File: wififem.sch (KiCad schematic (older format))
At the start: 44 parts, among them J1 Conn_Coaxial, J2 Conn_Coaxial, J3 Conn_Coaxial, J4 Conn_01x05, U1 MCP6566, U2 74HCT04, U3 SE2611T, U4 AP1117-15

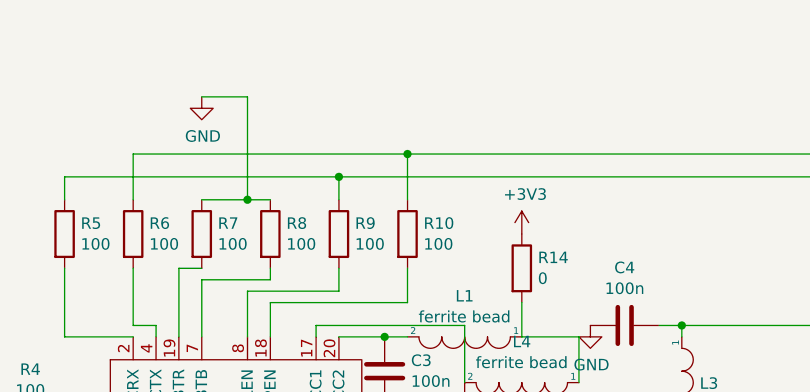
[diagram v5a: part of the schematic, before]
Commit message: Add LNA on/off jumper
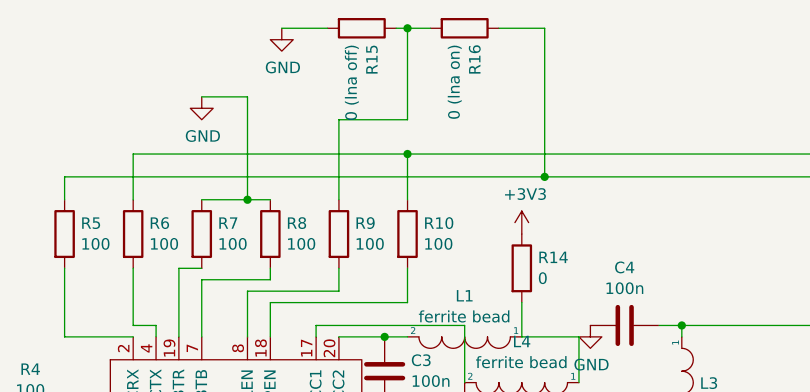
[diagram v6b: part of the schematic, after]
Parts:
- added R15: 0 (lna off), Resistors_SMD:R_0603, symbol device:R
- added R16: 0 (lna on), Resistors_SMD:R_0603, symbol device:R
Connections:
- wire segments 85 -> 91
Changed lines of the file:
@@
 	5700 2000 5700 1800
 Wire Wire Line
-	5700 1800 6100 1800
-Wire Wire Line
 	6100 1800 6100 1700
 Wire Wire Line
@@
 Wire Wire Line
 	5800 1850 5800 2000
-Wire Wire Line
-	6100 1400 6100 1300
 Wire Wire Line
 	4900 1300 8450 1300
@@
 	8450 1300 8450 3950
 Connection ~ 8450 3950
-Connection ~ 6100 1300
 Wire Wire Line
 	9100 3950 9100 1200
@@
 Connection ~ 7600 1950
 $Comp
-L power:GND #PWR?
+L power:GND #PWR028
 U 1 1 5A15FD74
 P 5300 3200
-F 0 "#PWR?" H 5300 2950 50  0001 C CNN
+F 0 "#PWR028" H 5300 2950 50  0001 C CNN
 F 1 "GND" H 5305 3027 50  0000 C CNN
 F 2 "" H 5300 3200 50  0001 C CNN
@@
 Wire Wire Line
 	5300 3200 5300 3150
+$Comp
+L device:R R15
+U 1 1 5A16EBBC
+P 6200 650
+F 0 "R15" H 6270 696 50  0000 L CNN
+F 1 "0 (lna off)" H 6270 605 50  0000 L CNN
+F 2 "Resistors_SMD:R_0603" V 6130 650 50  0001 C CNN
+F 3 "" H 6200 650 50  0001 C CNN
+	1    6200 650
+	0    1    1    0
+$EndComp
+$Comp
+L power:GND #PWR030
+U 1 1 5A172D6A
+P 5850 650
+F 0 "#PWR030" H 5850 400 50  0001 C CNN
+F 1 "GND" H 5855 477 50  0000 C CNN
+F 2 "" H 5850 650 50  0001 C CNN
+F 3 "" H 5850 650 50  0001 C CNN
+	1    5850 650
+	1    0    0    -1
+$EndComp
+Wire Wire Line
+	5850 650  6050 650
+Wire Wire Line
+	5700 1800 6100 1800
+$Comp
+L device:R R16
+U 1 1 5A17F845
+P 6650 650
+F 0 "R16" H 6720 696 50  0000 L CNN
+F 1 "0 (lna on)" H 6720 605 50  0000 L CNN
+F 2 "Resistors_SMD:R_0603" V 6580 650 50  0001 C CNN
+F 3 "" H 6650 650 50  0001 C CNN
+	1    6650 650
+	0    1    1    0
+$EndComp
+Wire Wire Line
+	7000 1300 7000 650
+Wire Wire Line
+	7000 650  6800 650
+Connection ~ 7000 1300
+Wire Wire Line
+	6100 1400 6100 1050
+Wire Wire Line
+	6100 1050 6400 1050
+Wire Wire Line
+	6400 1050 6400 650
+Wire Wire Line
+	6350 650  6500 650
+Connection ~ 6400 650
 $EndSCHEMATC

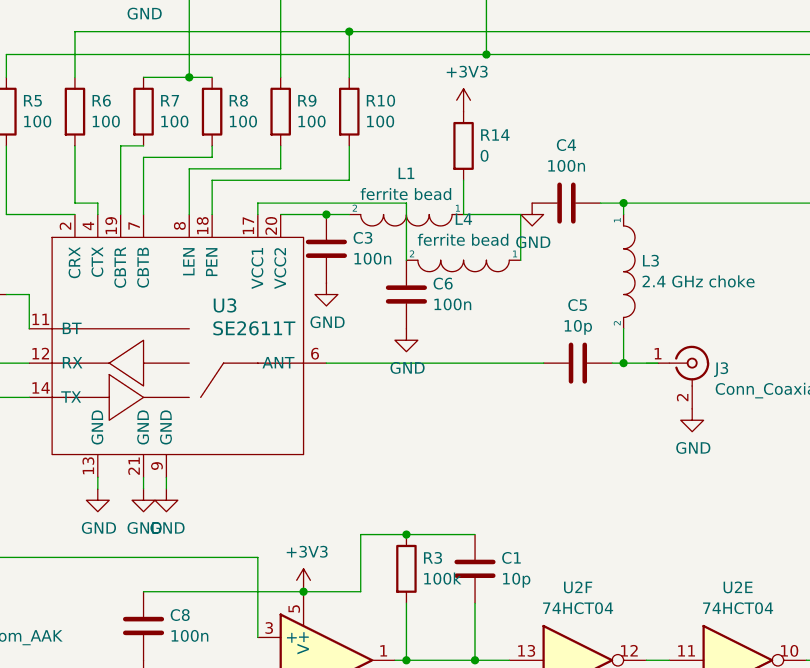
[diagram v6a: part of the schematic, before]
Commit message: Power supply decoupling as suggested
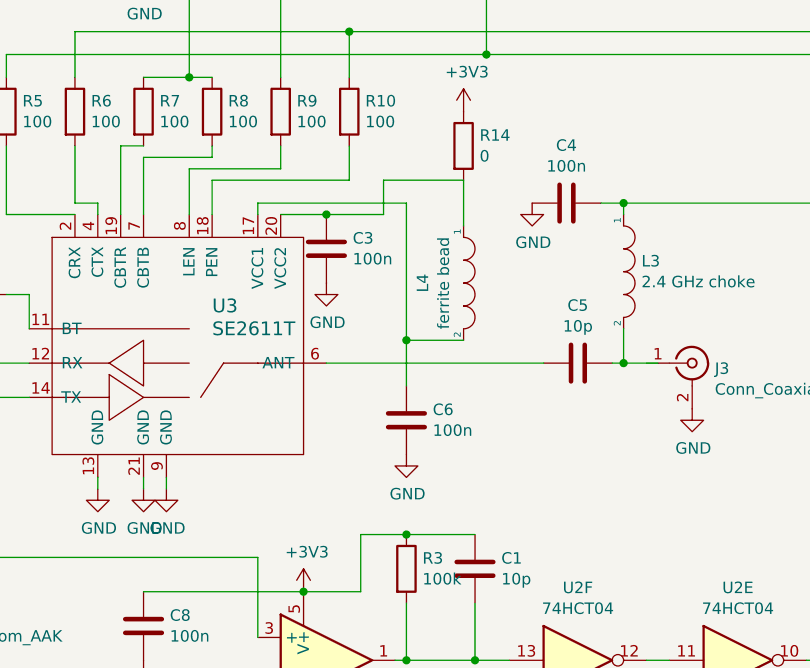
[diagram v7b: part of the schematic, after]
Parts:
- removed L1: ferrite bead, Inductors_SMD:L_0805_HandSoldering, symbol pspice:INDUCTOR
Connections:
- wire segments 91 -> 92
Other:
- moved on the sheet: C6, L4
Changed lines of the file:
@@
-$EndComp
-$Comp
-L pspice:INDUCTOR L1
-U 1 1 5A17AD26
-P 6650 2000
-F 0 "L1" H 6650 1822 50  0000 C CNN
-F 1 "ferrite bead" H 6650 1913 50  0000 C CNN
-F 2 "Inductors_SMD:L_0805_HandSoldering" H 6650 2000 50  0001 C CNN
-F 3 "" H 6650 2000 50  0001 C CNN
-	1    6650 2000
-	-1   0    0    1
 $EndComp
 $Comp
@@
 L device:C C6
 U 1 1 5A184860
-P 6650 2350
-F 0 "C6" H 6535 2304 50  0000 R CNN
-F 1 "100n" H 6535 2395 50  0000 R CNN
-F 2 "Capacitors_SMD:C_0805_HandSoldering" H 6688 2200 50  0001 C CNN
-F 3 "" H 6650 2350 50  0001 C CNN
-	1    6650 2350
+P 6650 2900
+F 0 "C6" H 6535 2854 50  0000 R CNN
+F 1 "100n" H 6535 2945 50  0000 R CNN
+F 2 "Capacitors_SMD:C_0805_HandSoldering" H 6688 2750 50  0001 C CNN
+F 3 "" H 6650 2900 50  0001 C CNN
+	1    6650 2900
 	-1   0    0    1
 $EndComp
@@
 L power:GND #PWR016
 U 1 1 5A1848E9
-P 6650 2500
-F 0 "#PWR016" H 6650 2250 50  0001 C CNN
-F 1 "GND" H 6655 2327 50  0000 C CNN
-F 2 "" H 6650 2500 50  0001 C CNN
-F 3 "" H 6650 2500 50  0001 C CNN
-	1    6650 2500
+P 6650 3050
+F 0 "#PWR016" H 6650 2800 50  0001 C CNN
+F 1 "GND" H 6655 2877 50  0000 C CNN
+F 2 "" H 6650 3050 50  0001 C CNN
+F 3 "" H 6650 3050 50  0001 C CNN
+	1    6650 3050
 	1    0    0    -1
 $EndComp
@@
 L pspice:INDUCTOR L4
 U 1 1 5A18492E
-P 6900 2200
-F 0 "L4" H 6900 2022 50  0000 C CNN
-F 1 "ferrite bead" H 6900 2113 50  0000 C CNN
-F 2 "Inductors_SMD:L_0805_HandSoldering" H 6900 2200 50  0001 C CNN
-F 3 "" H 6900 2200 50  0001 C CNN
-	1    6900 2200
-	-1   0    0    1
+P 6900 2300
+F 0 "L4" H 6900 2122 50  0000 C CNN
+F 1 "ferrite bead" H 6900 2213 50  0000 C CNN
+F 2 "Inductors_SMD:L_0805_HandSoldering" H 6900 2300 50  0001 C CNN
+F 3 "" H 6900 2300 50  0001 C CNN
+	1    6900 2300
+	0    1    1    0
 $EndComp
 $Comp
@@
 	-1   0    0    1
 $EndComp
-Wire Wire Line
-	8400 3950 8500 3950
-Wire Wire Line
-	7800 3950 7700 3950
-Wire Wire Line
-	6600 3950 7100 3950
-Wire Wire Line
-	6950 3700 6950 3950
-Connection ~ 6950 3950
-Wire Wire Line
-	6650 3700 6650 3950
-Connection ~ 6650 3950
-Wire Wire Line
-	6450 3400 6950 3400
-Connection ~ 6650 3400
-Wire Wire Line
-	5500 3650 6450 3650
-Wire Wire Line
-	6450 3400 6450 3650
-Wire Wire Line
-	5500 3200 5500 3150
-Wire Wire Line
-	5600 3200 5600 3150
-Wire Wire Line
-	5200 2000 4900 2000
-Wire Wire Line
-	4900 2000 4900 1700
-Wire Wire Line
-	5200 1700 5200 1950
-Wire Wire Line
-	5200 1950 5300 1950
-Wire Wire Line
-	5300 1950 5300 2000
-Wire Wire Line
-	5400 2000 5400 1700
-Wire Wire Line
-	5400 1700 5500 1700
-Wire Wire Line
-	5800 1700 5800 1750
-Wire Wire Line
-	5800 1750 5500 1750
-Wire Wire Line
-	5500 1750 5500 2000
-Wire Wire Line
-	5700 2000 5700 1800
-Wire Wire Line
-	6100 1800 6100 1700
-Wire Wire Line
-	6400 1700 6400 1850
-Wire Wire Line
-	6400 1850 5800 1850
-Wire Wire Line
-	5800 1850 5800 2000
-Wire Wire Line
-	4900 1300 8450 1300
-Wire Wire Line
-	4900 1300 4900 1400
-Wire Wire Line
-	5200 1400 5200 1200
-Wire Wire Line
-	5200 1200 9100 1200
-Wire Wire Line
-	6400 1200 6400 1400
-Wire Wire Line
-	5500 1400 5800 1400
-Wire Wire Line
-	5700 1400 5700 950
-Wire Wire Line
-	5700 950  5500 950
-Connection ~ 5700 1400
-Wire Wire Line
-	8450 1300 8450 3950
-Connection ~ 8450 3950
-Wire Wire Line
-	9100 3950 9100 1200
-Connection ~ 6400 1200
-Wire Wire Line
-	7550 2650 7750 2650
-Wire Wire Line
-	7250 2650 6300 2650
-Connection ~ 7600 2650
-Wire Wire Line
-	7500 1950 9250 1950
-Wire Wire Line
-	7600 2500 7600 2650
-Wire Wire Line
-	4100 2800 5000 2800
-Wire Wire Line
-	3800 2650 5000 2650
-Wire Wire Line
-	4550 2350 4600 2350
-Wire Wire Line
-	5000 2500 5000 2350
-Wire Wire Line
-	5000 2350 4900 2350
-Connection ~ 6300 2000
-Wire Wire Line
-	6100 2000 6400 2000
-Wire Wire Line
-	6900 2000 7150 2000
-Wire Wire Line
-	7150 2000 7150 2200
-Wire Wire Line
-	6650 2200 6650 1950
-Wire Wire Line
-	6650 1950 6000 1950
-Wire Wire Line
-	6000 1950 6000 2000
-Wire Wire Line
-	4150 2800 4150 2950
-Wire Wire Line
-	4150 3250 4150 3500
-Wire Wire Line
-	3900 3500 4350 3500
-Wire Wire Line
-	3900 4100 4350 4100
-Wire Wire Line
-	4650 3500 6000 3500
-Wire Wire Line
-	6000 3500 6000 3850
-Wire Wire Line
-	6000 4050 4650 4050
-Wire Wire Line
-	4650 4050 4650 4100
-Connection ~ 4150 3500
-Connection ~ 4150 4100
-Wire Wire Line
-	3600 3500 3600 4100
-Wire Wire Line
-	3400 3850 3600 3850
-Connection ~ 3600 3850
-Wire Wire Line
-	6000 4900 5900 4900
-Wire Wire Line
-	5600 5250 5600 5200
-Wire Wire Line
-	4250 4900 5300 4900
-Connection ~ 6200 3650
-Wire Wire Line
-	7650 4550 7100 4550
-Wire Wire Line
-	7100 4550 7100 4850
-Wire Wire Line
-	7650 5550 7100 5550
-Wire Wire Line
-	7100 5550 7100 5150
-Connection ~ 4150 2800
-Connection ~ 4700 2800
-Wire Wire Line
-	9650 2100 9650 3300
-Connection ~ 9650 2700
-Wire Wire Line
-	6900 1850 6900 2000
-Wire Wire Line
-	3550 4550 3550 5000
-Wire Wire Line
-	3550 4950 3500 4950
-Wire Wire Line
-	3550 4550 3500 4550
-Connection ~ 3550 4950
-Wire Wire Line
-	3500 4750 3550 4750
-Connection ~ 3550 4750
-Wire Wire Line
-	3500 4650 3750 4650
-Wire Wire Line
-	3750 4650 3750 4550
-Wire Wire Line
-	3500 4850 3750 4850
-Wire Wire Line
-	3750 4850 3750 4900
-Connection ~ 5000 4900
-Connection ~ 4500 4900
-Wire Wire Line
-	4250 4550 6800 4550
-Wire Wire Line
-	6800 4550 6800 5850
-Wire Wire Line
-	6800 5850 9250 5850
-Wire Wire Line
-	9250 5850 9250 1950
 $Comp
 L pspice:INDUCTOR L2
@@
 	1    0    0    -1
 $EndComp
-Wire Wire Line
-	7600 2000 7600 1950
-Connection ~ 7600 1950
 $Comp
 L power:GND #PWR028
@@
 	1    0    0    -1
 $EndComp
-Wire Wire Line
-	5300 3200 5300 3150
 $Comp
 L device:R R15
@@
 	1    0    0    -1
 $EndComp
-Wire Wire Line
-	5850 650  6050 650
-Wire Wire Line
-	5700 1800 6100 1800
 $Comp
 L device:R R16
@@
 $EndComp
 Wire Wire Line
+	8400 3950 8500 3950
+Wire Wire Line
+	7800 3950 7700 3950
+Wire Wire Line
+	6600 3950 7100 3950
+Wire Wire Line
+	6950 3700 6950 3950
+Connection ~ 6950 3950
+Wire Wire Line
+	6650 3700 6650 3950
+Connection ~ 6650 3950
+Wire Wire Line
+	6450 3400 6950 3400
+Connection ~ 6650 3400
+Wire Wire Line
+	5500 3650 6450 3650
+Wire Wire Line
+	6450 3400 6450 3650
+Wire Wire Line
+	5500 3200 5500 3150
+Wire Wire Line
+	5600 3200 5600 3150
+Wire Wire Line
+	5200 2000 4900 2000
+Wire Wire Line
+	4900 2000 4900 1700
+Wire Wire Line
+	5200 1700 5200 1950
+Wire Wire Line
+	5200 1950 5300 1950
+Wire Wire Line
+	5300 1950 5300 2000
+Wire Wire Line
+	5400 2000 5400 1700
+Wire Wire Line
+	5400 1700 5500 1700
+Wire Wire Line
+	5800 1700 5800 1750
+Wire Wire Line
+	5800 1750 5500 1750
+Wire Wire Line
+	5500 1750 5500 2000
+Wire Wire Line
+	5700 2000 5700 1800
+Wire Wire Line
+	6100 1800 6100 1700
+Wire Wire Line
+	6400 1700 6400 1850
+Wire Wire Line
+	6400 1850 5800 1850
+Wire Wire Line
+	5800 1850 5800 2000
+Wire Wire Line
+	4900 1300 8450 1300
+Wire Wire Line
+	4900 1300 4900 1400
+Wire Wire Line
+	5200 1400 5200 1200
+Wire Wire Line
+	5200 1200 9100 1200
+Wire Wire Line
+	6400 1200 6400 1400
+Wire Wire Line
+	5500 1400 5800 1400
+Wire Wire Line
+	5700 1400 5700 950
+Wire Wire Line
+	5700 950  5500 950
+Connection ~ 5700 1400
+Wire Wire Line
+	8450 1300 8450 3950
+Connection ~ 8450 3950
+Wire Wire Line
+	9100 3950 9100 1200
+Connection ~ 6400 1200
+Wire Wire Line
+	7550 2650 7750 2650
+Wire Wire Line
+	7250 2650 6300 2650
+Connection ~ 7600 2650
+Wire Wire Line
+	7500 1950 9250 1950
+Wire Wire Line
+	7600 2500 7600 2650
+Wire Wire Line
+	4100 2800 5000 2800
+Wire Wire Line
+	4550 2350 4600 2350
+Wire Wire Line
+	5000 2500 5000 2350
+Wire Wire Line
+	5000 2350 4900 2350
+Connection ~ 6300 2000
+Wire Wire Line
+	6100 2000 6550 2000
+Wire Wire Line
+	6650 1950 6650 2750
+Wire Wire Line
+	6650 1950 6000 1950
+Wire Wire Line
+	6000 1950 6000 2000
+Wire Wire Line
+	4150 2800 4150 2950
+Wire Wire Line
+	4150 3250 4150 3500
+Wire Wire Line
+	3900 3500 4350 3500
+Wire Wire Line
+	3900 4100 4350 4100
+Wire Wire Line
+	4650 3500 6000 3500
+Wire Wire Line
+	6000 3500 6000 3850
+Wire Wire Line
+	6000 4050 4650 4050
+Wire Wire Line
+	4650 4050 4650 4100
+Connection ~ 4150 3500
+Connection ~ 4150 4100
+Wire Wire Line
+	3600 3500 3600 4100
+Wire Wire Line
+	3400 3850 3600 3850
+Connection ~ 3600 3850
+Wire Wire Line
+	6000 4900 5900 4900
+Wire Wire Line
+	5600 5250 5600 5200
+Wire Wire Line
+	4250 4900 5300 4900
+Connection ~ 6200 3650
+Wire Wire Line
+	7650 4550 7100 4550
+Wire Wire Line
+	7100 4550 7100 4850
+Wire Wire Line
+	7650 5550 7100 5550
+Wire Wire Line
+	7100 5550 7100 5150
+Connection ~ 4150 2800
+Connection ~ 4700 2800
+Wire Wire Line
+	9650 2100 9650 3300
+Connection ~ 9650 2700
+Wire Wire Line
+	6900 1850 6900 2050
+Wire Wire Line
+	3550 4550 3550 5000
+Wire Wire Line
+	3550 4950 3500 4950
+Wire Wire Line
+	3550 4550 3500 4550
+Connection ~ 3550 4950
+Wire Wire Line
+	3500 4750 3550 4750
+Connection ~ 3550 4750
+Wire Wire Line
+	3500 4650 3750 4650
+Wire Wire Line
+	3750 4650 3750 4550
+Wire Wire Line
+	3500 4850 3750 4850
+Wire Wire Line
+	3750 4850 3750 4900
+Connection ~ 5000 4900
+Connection ~ 4500 4900
+Wire Wire Line
+	4250 4550 6800 4550
+Wire Wire Line
+	6800 4550 6800 5850
+Wire Wire Line
+	6800 5850 9250 5850
+Wire Wire Line
+	9250 5850 9250 1950
+Wire Wire Line
+	7600 2000 7600 1950
+Connection ~ 7600 1950
+Wire Wire Line
+	5300 3200 5300 3150
+Wire Wire Line
+	5850 650  6050 650
+Wire Wire Line
+	5700 1800 6100 1800
+Wire Wire Line
 	7000 1300 7000 650
 Wire Wire Line
@@
 	6350 650  6500 650
 Connection ~ 6400 650
+Wire Wire Line
+	6550 2000 6550 1850
+Wire Wire Line
+	6550 1850 6900 1850
+Wire Wire Line
+	6900 2550 6650 2550
+Connection ~ 6650 2550
+Wire Wire Line
+	3800 2650 5000 2650
 $EndSCHEMATC

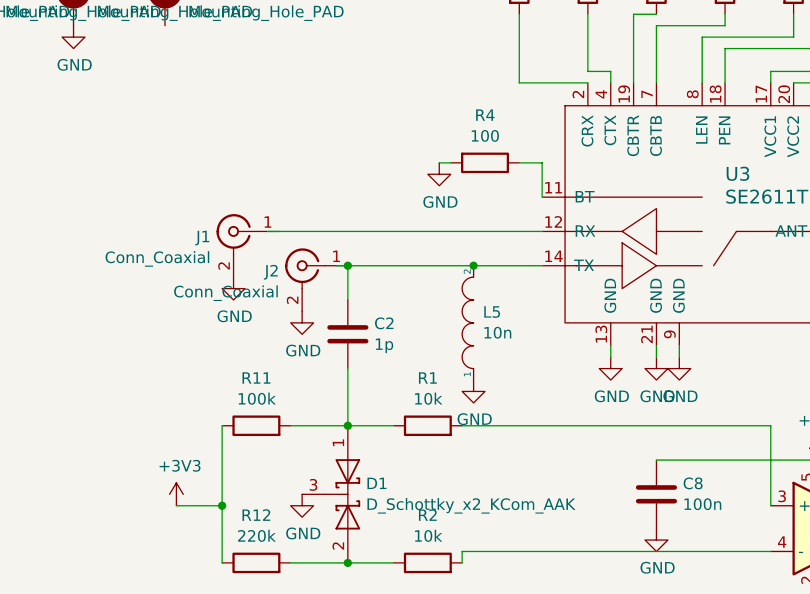
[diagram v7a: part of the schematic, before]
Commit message: Add DC block capacitors in all RF ports
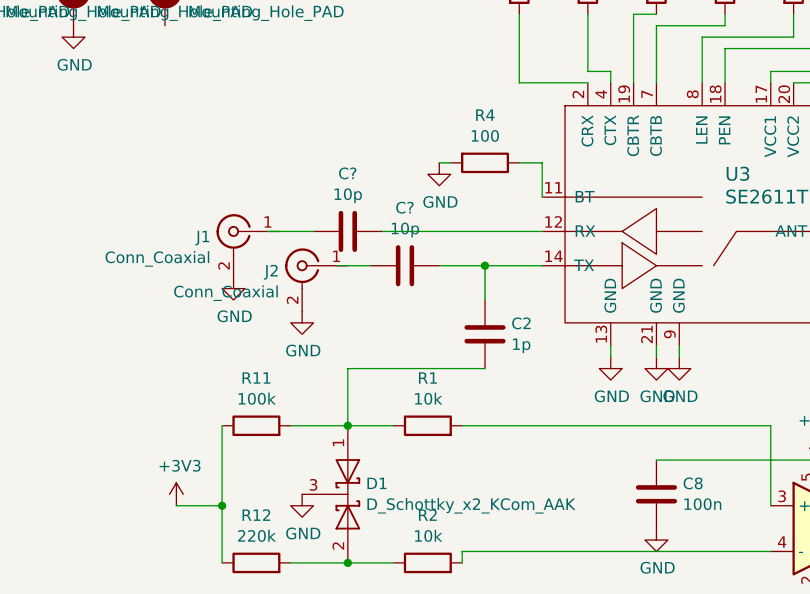
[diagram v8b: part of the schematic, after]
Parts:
- removed L5: 10n, Inductors_SMD:L_0805_HandSoldering, symbol pspice:INDUCTOR
- added C? (x2): 10p, Capacitors_SMD:C_0805_HandSoldering, symbol device:C
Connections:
- wire segments 92 -> 95
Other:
- moved on the sheet: C2
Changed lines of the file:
@@
 L device:C C2
 U 1 1 5A16FCB3
-P 4150 3100
-F 0 "C2" H 4035 3054 50  0000 R CNN
-F 1 "1p" H 4035 3145 50  0000 R CNN
-F 2 "Capacitors_SMD:C_0805_HandSoldering" H 4188 2950 50  0001 C CNN
-F 3 "" H 4150 3100 50  0001 C CNN
-	1    4150 3100
+P 4750 3100
+F 0 "C2" H 4635 3054 50  0000 R CNN
+F 1 "1p" H 4635 3145 50  0000 R CNN
+F 2 "Capacitors_SMD:C_0805_HandSoldering" H 4788 2950 50  0001 C CNN
+F 3 "" H 4750 3100 50  0001 C CNN
+	1    4750 3100
 	-1   0    0    1
 $EndComp
@@
 $EndComp
 $Comp
-L pspice:INDUCTOR L5
-U 1 1 5A1BC783
-P 4700 3050
-F 0 "L5" V 4746 3010 50  0000 R CNN
-F 1 "10n" V 4655 3010 50  0000 R CNN
-F 2 "Inductors_SMD:L_0805_HandSoldering" H 4700 3050 50  0001 C CNN
-F 3 "" H 4700 3050 50  0001 C CNN
-	1    4700 3050
-	0    -1   -1   0
-$EndComp
-$Comp
-L power:GND #PWR017
-U 1 1 5A1C03BF
-P 4700 3300
-F 0 "#PWR017" H 4700 3050 50  0001 C CNN
-F 1 "GND" H 4705 3127 50  0000 C CNN
-F 2 "" H 4700 3300 50  0001 C CNN
-F 3 "" H 4700 3300 50  0001 C CNN
-	1    4700 3300
-	1    0    0    -1
-$EndComp
-$Comp
 L Logic_74xx:74HCT04 U2
 U 4 1 5A1C573B
@@
 	7600 2500 7600 2650
 Wire Wire Line
-	4100 2800 5000 2800
-Wire Wire Line
 	4550 2350 4600 2350
 Wire Wire Line
@@
 Wire Wire Line
 	6000 1950 6000 2000
-Wire Wire Line
-	4150 2800 4150 2950
-Wire Wire Line
-	4150 3250 4150 3500
 Wire Wire Line
 	3900 3500 4350 3500
@@
 Wire Wire Line
 	7100 5550 7100 5150
-Connection ~ 4150 2800
-Connection ~ 4700 2800
 Wire Wire Line
 	9650 2100 9650 3300
@@
 	6900 2550 6650 2550
 Connection ~ 6650 2550
-Wire Wire Line
-	3800 2650 5000 2650
+$Comp
+L device:C C?
+U 1 1 5A1C7E8A
+P 4150 2650
+F 0 "C?" V 3898 2650 50  0000 C CNN
+F 1 "10p" V 3989 2650 50  0000 C CNN
+F 2 "Capacitors_SMD:C_0805_HandSoldering" H 4188 2500 50  0001 C CNN
+F 3 "" H 4150 2650 50  0001 C CNN
+	1    4150 2650
+	0    1    1    0
+$EndComp
+Wire Wire Line
+	4750 2800 4750 2950
+Connection ~ 4750 2800
+Wire Wire Line
+	4750 3250 4150 3250
+Wire Wire Line
+	4150 3250 4150 3500
+$Comp
+L device:C C?
+U 1 1 5A1D3989
+P 4400 2800
+F 0 "C?" V 4148 2800 50  0000 C CNN
+F 1 "10p" V 4239 2800 50  0000 C CNN
+F 2 "Capacitors_SMD:C_0805_HandSoldering" H 4438 2650 50  0001 C CNN
+F 3 "" H 4400 2800 50  0001 C CNN
+	1    4400 2800
+	0    1    1    0
+$EndComp
+Wire Wire Line
+	4250 2800 4100 2800
+Wire Wire Line
+	4550 2800 5000 2800
+Wire Wire Line
+	4000 2650 3800 2650
+Wire Wire Line
+	4300 2650 5000 2650
 $EndSCHEMATC
